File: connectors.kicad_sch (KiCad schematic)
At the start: 4 parts, among them J1 Conn_01x04_Pin, J2 Conn_01x04_Pin, J3 Conn_01x09_Pin, J4 Conn_02x03_Odd_Even

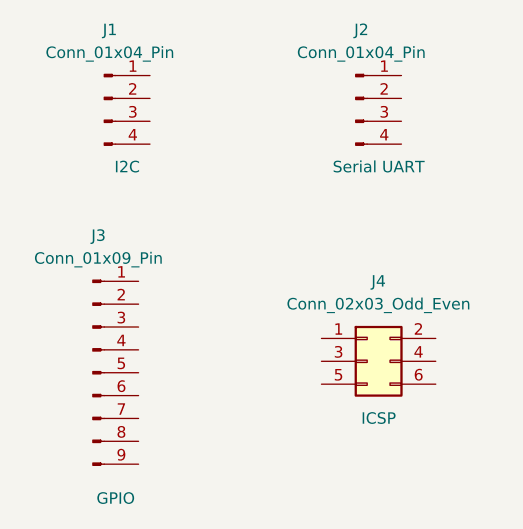
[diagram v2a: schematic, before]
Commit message: Completed wiring of main sheet.
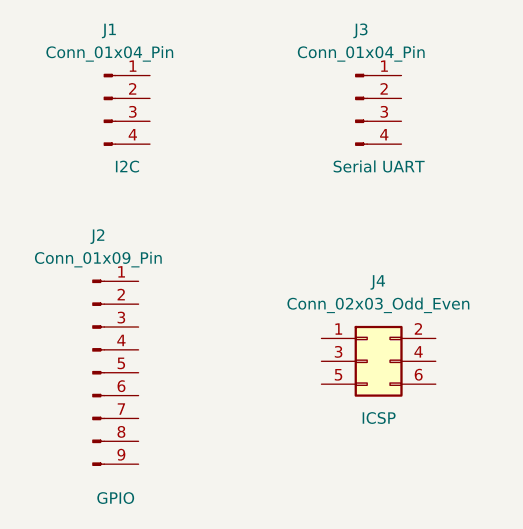
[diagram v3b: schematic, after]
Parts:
- J1: footprint (none) -> Connector_PinHeader_2.54mm:PinHeader_1x04_P2.54mm_Vertical
- J2: renamed from J3; footprint (none) -> Connector_PinHeader_2.54mm:PinHeader_1x09_P2.54mm_Vertical
- J3: renamed from J2; footprint (none) -> Connector_PinHeader_2.54mm:PinHeader_1x04_P2.54mm_Vertical
- J4: footprint (none) -> Connector_PinHeader_2.54mm:PinHeader_2x03_P2.54mm_Vertical
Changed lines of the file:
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@@
 			)
 		)
-		(property "Footprint" ""
+		(property "Footprint" "Connector_PinHeader_2.54mm:PinHeader_1x04_P2.54mm_Vertical"
 			(at 96.52 76.2 0)
 			(effects
@@
 			)
 		)
-		(property "Footprint" ""
+		(property "Footprint" "Connector_PinHeader_2.54mm:PinHeader_2x03_P2.54mm_Vertical"
 			(at 125.73 105.41 0)
 			(effects
@@
 		(on_board yes)
 		(dnp no)
-		(property "Reference" "J3"
+		(property "Reference" "J2"
 			(at 95.885 91.44 0)
 			(effects
@@
 			)
 		)
-		(property "Footprint" ""
+		(property "Footprint" "Connector_PinHeader_2.54mm:PinHeader_1x09_P2.54mm_Vertical"
 			(at 95.25 106.68 0)
 			(effects
@@
 			(project ""
 				(path "/be1eed37-8a6f-4061-89c1-54ae666185b6/b4f41415-82b1-4959-a14a-21198429c3d7"
-					(reference "J3")
+					(reference "J2")
 					(unit 1)
 				)
@@
 		(on_board yes)
 		(dnp no)
-		(property "Reference" "J2"
+		(property "Reference" "J3"
 			(at 125.095 68.58 0)
 			(effects
@@
 			)
 		)
-		(property "Footprint" ""
+		(property "Footprint" "Connector_PinHeader_2.54mm:PinHeader_1x04_P2.54mm_Vertical"
 			(at 124.46 76.2 0)
 			(effects
@@
 			(project "MCU_Datalogger"
 				(path "/be1eed37-8a6f-4061-89c1-54ae666185b6/b4f41415-82b1-4959-a14a-21198429c3d7"
-					(reference "J2")
-					(unit 1)
-				)
+					(reference "J3")
+					(unit 1)
+				)

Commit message: Completed wiring in the second sheet.
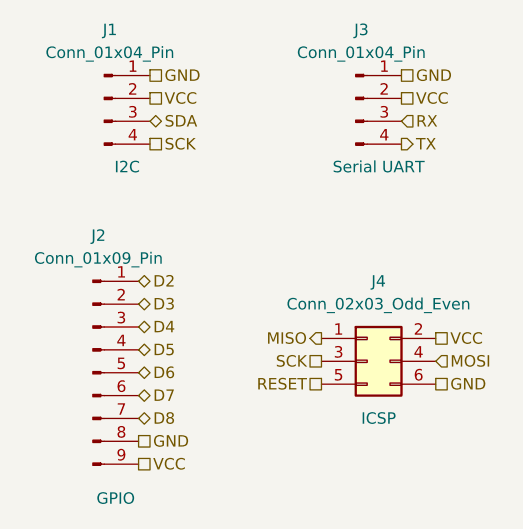
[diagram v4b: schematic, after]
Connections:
- net GND: now reaches J1.1 (Pin_1)
- net GND: now also J2.8 (Pin_8), J3.1 (Pin_1), J4.6 (Pin_6)
- net VCC: now reaches J1.2 (Pin_2)
- net VCC: now also J2.9 (Pin_9), J3.2 (Pin_2), J4.2 (Pin_2)
- net SDA: now reaches J1.3 (Pin_3)
- net SCK: now reaches J1.4 (Pin_4)
- net SCK: now also J4.3 (Pin_3)
- net MISO: now reaches J4.1 (Pin_1)
- net MOSI: now reaches J4.4 (Pin_4)
- net RESET: now reaches J4.5 (Pin_5)
- net D2: now reaches J2.1 (Pin_1)
- net D3: now reaches J2.2 (Pin_2)
- net D4: now reaches J2.3 (Pin_3)
- net D5: now reaches J2.4 (Pin_4)
- net D6: now reaches J2.5 (Pin_5)
- net D7: now reaches J2.6 (Pin_6)
- net D8: now reaches J2.7 (Pin_7)
- net RX: now reaches J3.3 (Pin_3)
- net TX: now reaches J3.4 (Pin_4)
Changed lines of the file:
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@@
 	(generator_version "9.0")
 	(paper "A4")
+	(hierarchical_label "VCC"
+		(shape passive)
+		(at 129.54 76.2 0)
+		(effects
+			(font
+				(size 1.27 1.27)
+			)
+			(justify left)
+		)
+	)
+	(hierarchical_label "D5"
+		(shape bidirectional)
+		(at 100.33 104.14 0)
+		(effects
+			(font
+				(size 1.27 1.27)
+			)
+			(justify left)
+		)
+	)
+	(hierarchical_label "VCC"
+		(shape passive)
+		(at 133.35 102.87 0)
+		(effects
+			(font
+				(size 1.27 1.27)
+			)
+			(justify left)
+		)
+	)
+	(hierarchical_label "SCK"
+		(shape passive)
+		(at 120.65 105.41 180)
+		(effects
+			(font
+				(size 1.27 1.27)
+			)
+			(justify right)
+		)
+	)
+	(hierarchical_label "GND"
+		(shape passive)
+		(at 133.35 107.95 0)
+		(effects
+			(font
+				(size 1.27 1.27)
+			)
+			(justify left)
+		)
+	)
+	(hierarchical_label "TX"
+		(shape output)
+		(at 129.54 81.28 0)
+		(effects
+			(font
+				(size 1.27 1.27)
+			)
+			(justify left)
+		)
+	)
+	(hierarchical_label "D6"
+		(shape bidirectional)
+		(at 100.33 106.68 0)
+		(effects
+			(font
+				(size 1.27 1.27)
+			)
+			(justify left)
+		)
+	)
+	(hierarchical_label "VCC"
+		(shape passive)
+		(at 101.6 76.2 0)
+		(effects
+			(font
+				(size 1.27 1.27)
+			)
+			(justify left)
+		)
+	)
+	(hierarchical_label "SDA"
+		(shape bidirectional)
+		(at 101.6 78.74 0)
+		(effects
+			(font
+				(size 1.27 1.27)
+			)
+			(justify left)
+		)
+	)
+	(hierarchical_label "D7"
+		(shape bidirectional)
+		(at 100.33 109.22 0)
+		(effects
+			(font
+				(size 1.27 1.27)
+			)
+			(justify left)
+		)
+	)
+	(hierarchical_label "RX"
+		(shape input)
+		(at 129.54 78.74 0)
+		(effects
+			(font
+				(size 1.27 1.27)
+			)
+			(justify left)
+		)
+	)
+	(hierarchical_label "MOSI"
+		(shape input)
+		(at 133.35 105.41 0)
+		(effects
+			(font
+				(size 1.27 1.27)
+			)
+			(justify left)
+		)
+	)
+	(hierarchical_label "GND"
+		(shape passive)
+		(at 129.54 73.66 0)
+		(effects
+			(font
+				(size 1.27 1.27)
+			)
+			(justify left)
+		)
+	)
+	(hierarchical_label "SCK"
+		(shape passive)
+		(at 101.6 81.28 0)
+		(effects
+			(font
+				(size 1.27 1.27)
+			)
+			(justify left)
+		)
+	)
+	(hierarchical_label "GND"
+		(shape passive)
+		(at 100.33 114.3 0)
+		(effects
+			(font
+				(size 1.27 1.27)
+			)
+			(justify left)
+		)
+	)
+	(hierarchical_label "VCC"
+		(shape passive)
+		(at 100.33 116.84 0)
+		(effects
+			(font
+				(size 1.27 1.27)
+			)
+			(justify left)
+		)
+	)
+	(hierarchical_label "MISO"
+		(shape output)
+		(at 120.65 102.87 180)
+		(effects
+			(font
+				(size 1.27 1.27)
+			)
+			(justify right)
+		)
+	)
+	(hierarchical_label "D3"
+		(shape bidirectional)
+		(at 100.33 99.06 0)
+		(effects
+			(font
+				(size 1.27 1.27)
+			)
+			(justify left)
+		)
+	)
+	(hierarchical_label "GND"
+		(shape passive)
+		(at 101.6 73.66 0)
+		(effects
+			(font
+				(size 1.27 1.27)
+			)
+			(justify left)
+		)
+	)
+	(hierarchical_label "D8"
+		(shape bidirectional)
+		(at 100.33 111.76 0)
+		(effects
+			(font
+				(size 1.27 1.27)
+			)
+			(justify left)
+		)
+	)
+	(hierarchical_label "D2"
+		(shape bidirectional)
+		(at 100.33 96.52 0)
+		(effects
+			(font
+				(size 1.27 1.27)
+			)
+			(justify left)
+		)
+	)
+	(hierarchical_label "RESET"
+		(shape passive)
+		(at 120.65 107.95 180)
+		(effects
+			(font
+				(size 1.27 1.27)
+			)
+			(justify right)
+		)
+	)
+	(hierarchical_label "D4"
+		(shape bidirectional)
+		(at 100.33 101.6 0)
+		(effects
+			(font
+				(size 1.27 1.27)
+			)
+			(justify left)
+		)
+	)
 	(symbol
 		(lib_id "Connector:Conn_01x04_Pin")

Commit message: Fixed two defects in the schematic.
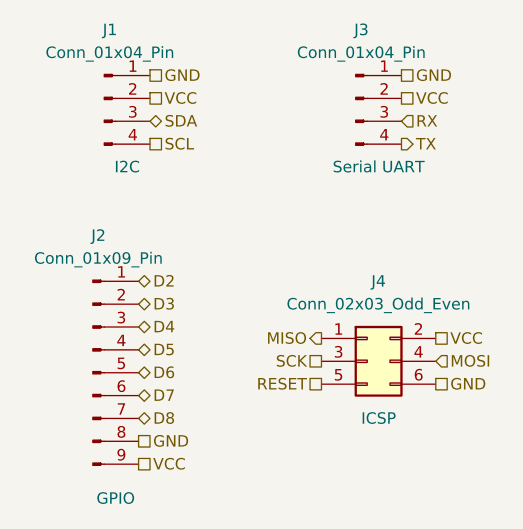
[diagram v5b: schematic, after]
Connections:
- net SCK: no longer J1.4 (Pin_4)
- new net SCL: J1.4 (Pin_4)
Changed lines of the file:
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@@
 		)
 	)
-	(hierarchical_label "SCK"
+	(hierarchical_label "SCL"
 		(shape passive)
 		(at 101.6 81.28 0)
